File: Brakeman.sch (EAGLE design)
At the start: 9 parts

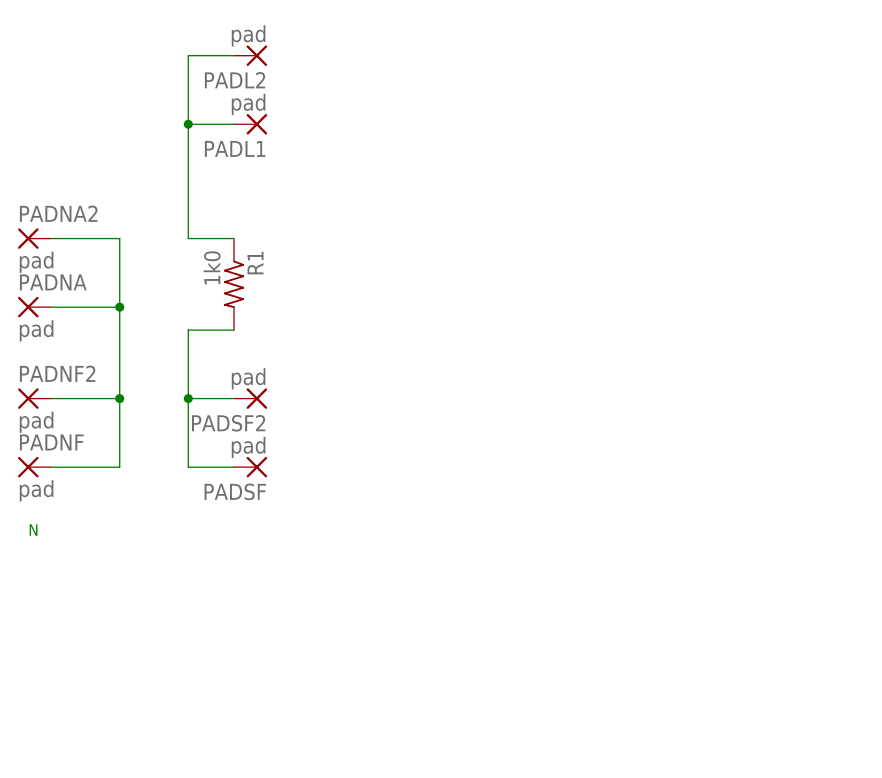
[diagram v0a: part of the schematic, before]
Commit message: added foot tiedowns
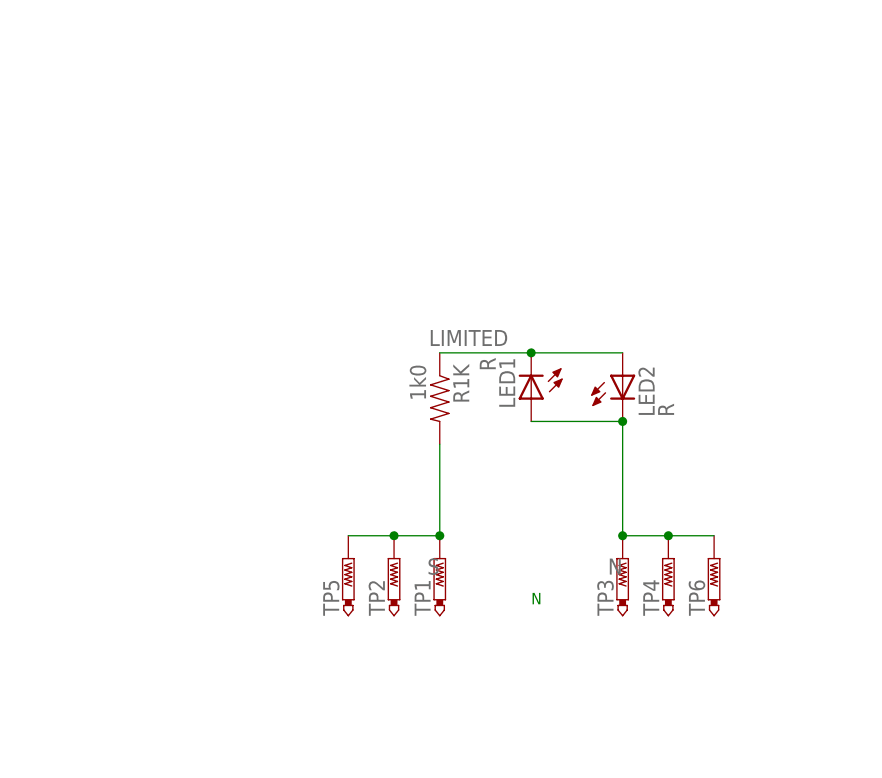
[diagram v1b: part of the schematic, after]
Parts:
- removed PADL1, PADL2, PADNA, PADNA2, PADNF, PADNF2, PADSF, PADSF2: pad, wirepad:SMD2
- removed R1: 1k0, resistor:R-US_0204/5
- added LED1, LED2: R, SPCoast:LED0603-LED
- added R1K: 1k0, SPCoast:R0603-RES
- added TP1, TP2, TP3, TP4, TP5, TP6: PTR1PAD1-13, testpad:PTR1PAD1-13
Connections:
- net LIMITED: now also LED1.C, LED2.A, R1K.1; no longer PADL1.P, PADL2.P, R1.1
- net N: now also LED1.A, LED2.C, TP3.TP, TP4.TP, TP6.TP; no longer PADNA.P, PADNA2.P, PADNF.P, PADNF2.P
- net S: now also R1K.2, TP1.TP, TP2.TP, TP5.TP; no longer PADSF.P, PADSF2.P, R1.2
